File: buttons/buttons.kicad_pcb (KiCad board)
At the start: 2 copper layers, 9 parts, among them J1 header

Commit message: cleaned up directories, silkscreen
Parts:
- added H1: MountingHole, buttons:MountingHole_2.5mm_Pad, F.Cu at (109.9, 71.6)
- added H2: MountingHole, buttons:MountingHole_2.5mm_Pad, F.Cu at (141.9, 71.7)
- J1: footprint SamacSys_Parts:HDRV9W63P0X254_1X9_2286X369X950P -> buttons:header
- S1, S2: footprint SamacSys_Parts:OS103011MS8QP1 -> buttons:switch
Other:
- board outline added: 42 x 20.1 mm
- board text added: "ECE 477 Group 14 Switch Board Rev. 1"

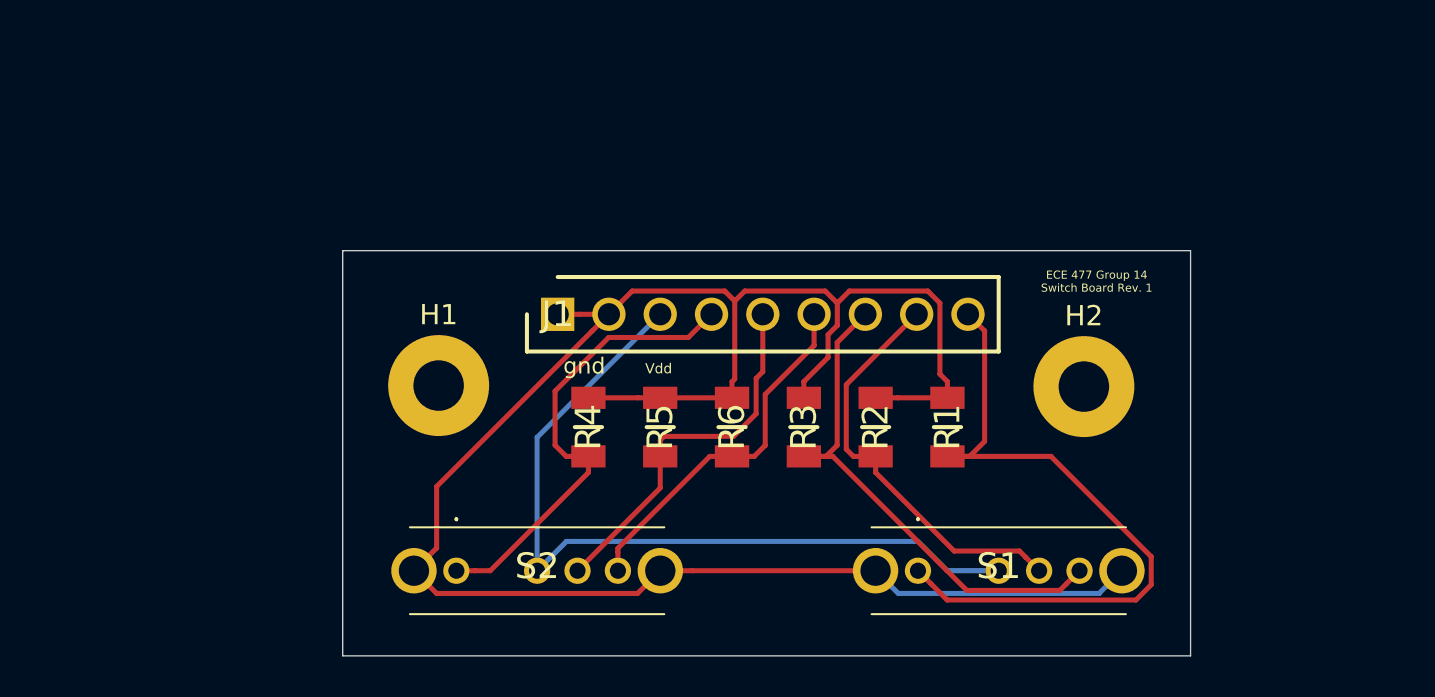
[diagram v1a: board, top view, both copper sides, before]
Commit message: Added reset button, fixed 7seg pin order
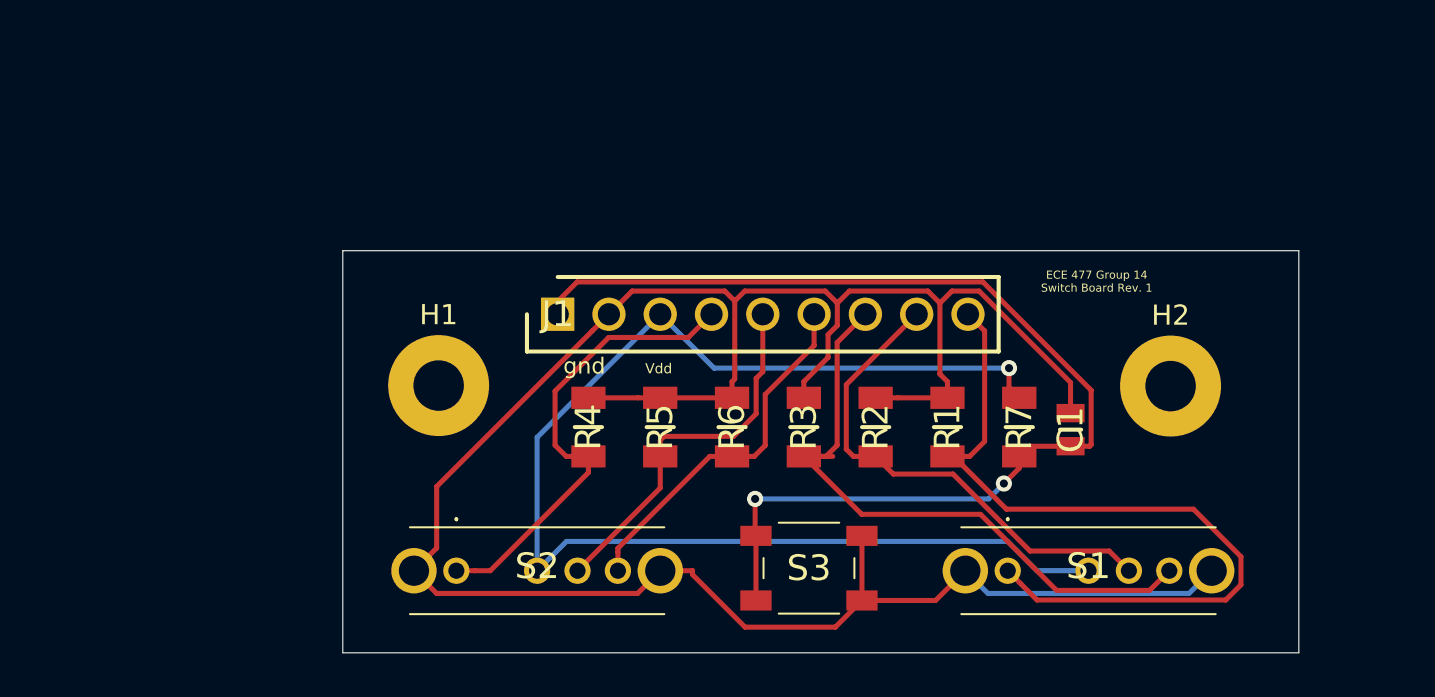
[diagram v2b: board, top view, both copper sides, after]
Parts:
- added C1: CL21B104KBCNNNC, SamacSys_Parts:CAPC2012X95N, F.Cu at (141.2, 73.8)
- added R7: 100k, SamacSys_Parts:RESC3116X70N, F.Cu at (138.7, 73.7)
- added S3: PTS647SM50SMTR2LFS, SamacSys_Parts:PTS647SM50SMTR2LFS, F.Cu at (128.3, 80.6)
- moved S1 4.44 mm to (142.1, 80.8)
- moved H2 4.29 mm to (146.2, 71.6)
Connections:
- J1 pad 1: /gnd -> Net-(C1-Pad1)
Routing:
- net Net-(C1-Pad1): track 0.00 -> 56.1 mm, vias 0 -> 2
- net /Vdd: track 39.3 -> 63.8 mm, vias 0 -> 1
- net /gnd: track 99.9 -> 117.6 mm
- net Net-(J1-Pad7): track 25.7 -> 31.6 mm
- net Net-(J1-Pad9): track 34.8 -> 39.2 mm
- net Net-(J1-Pad8): track 20.6 -> 24.6 mm
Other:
- board size 42 x 20.1 mm -> 47.3 x 19.9 mm

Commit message: final Rev1 changes. increased heatsink area, flipped LEDs again, increased button mount hole size
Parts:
- H1, H2: footprint buttons:MountingHole_2.5mm_Pad -> buttons:MountingHole_3.2mm_M3_Pad
- moved H2 2.18 mm to (147.9, 72.9)
- moved H1 1.37 mm to (109.7, 72.9)
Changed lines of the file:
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@@
-(kicad_pcb (version 20171130) (host pcbnew "(5.1.10)-1")
+(kicad_pcb (version 20171130) (host pcbnew "(5.1.5)-3")
   (general
     (thickness 1.6)
@@
     (add_net "Net-(J1-Pad9)")
   )
+  (module buttons:MountingHole_3.2mm_M3_Pad (layer F.Cu)
+    (at 147.9296 72.9234)
+    (descr "Mounting Hole 3.2mm, M3")
+    (tags "mounting hole 3.2mm m3")
+    (attr virtual)
+    (fp_text reference H2 (at 0 -4.2) (layer F.SilkS)
+      (effects (font (size 1 1) (thickness 0.15)))
+    )
+    (fp_text value MountingHole (at 0 4.2) (layer F.Fab)
+      (effects (font (size 1 1) (thickness 0.15)))
+    )
+    (fp_circle (center 0 0) (end 3.45 0) (layer F.CrtYd) (width 0.05))
+    (fp_circle (center 0 0) (end 3.2 0) (layer Cmts.User) (width 0.15))
+    (fp_text user %R (at 0.3 0) (layer F.Fab)
+      (effects (font (size 1 1) (thickness 0.15)))
+    )
+    (pad 1 thru_hole circle (at 0 0) (size 6.4 6.4) (drill 3.2) (layers *.Cu *.Mask))
+  )
+  (module buttons:MountingHole_3.2mm_M3_Pad (layer F.Cu)
+    (at 109.6518 72.9488)
+    (descr "Mounting Hole 3.2mm, M3")
+    (tags "mounting hole 3.2mm m3")
+    (attr virtual)
+    (fp_text reference H1 (at 0 -4.2) (layer F.SilkS)
+      (effects (font (size 1 1) (thickness 0.15)))
+    )
+    (fp_text value MountingHole (at 0 4.2) (layer F.Fab)
+      (effects (font (size 1 1) (thickness 0.15)))
+    )
+    (fp_circle (center 0 0) (end 3.45 0) (layer F.CrtYd) (width 0.05))
+    (fp_circle (center 0 0) (end 3.2 0) (layer Cmts.User) (width 0.15))
+    (fp_text user %R (at 0.3 0) (layer F.Fab)
+      (effects (font (size 1 1) (thickness 0.15)))
+    )
+    (pad 1 thru_hole circle (at 0 0) (size 6.4 6.4) (drill 3.2) (layers *.Cu *.Mask))
+  )
   (module SamacSys_Parts:PTS647SM50SMTR2LFS (layer F.Cu)
     (at 128.27 80.645)
@@
       (effects (font (size 1.27 1.27) (thickness 0.254)))
     )
+    (fp_line (start 2.25 -0.5) (end 2.25 0.5) (layer F.SilkS) (width 0.1))
+    (fp_line (start -1.5 2.25) (end 1.5 2.25) (layer F.SilkS) (width 0.1))
+    (fp_line (start -2.25 -0.5) (end -2.25 0.5) (layer F.SilkS) (width 0.1))
+    (fp_line (start -1.5 -2.25) (end 1.5 -2.25) (layer F.SilkS) (width 0.1))
+    (fp_line (start -4.4 3.25) (end -4.4 -3.25) (layer F.CrtYd) (width 0.1))
+    (fp_line (start 4.4 3.25) (end -4.4 3.25) (layer F.CrtYd) (width 0.1))
+    (fp_line (start 4.4 -3.25) (end 4.4 3.25) (layer F.CrtYd) (width 0.1))
+    (fp_line (start -4.4 -3.25) (end 4.4 -3.25) (layer F.CrtYd) (width 0.1))
+    (fp_line (start -2.25 2.25) (end -2.25 -2.25) (layer F.Fab) (width 0.2))
+    (fp_line (start 2.25 2.25) (end -2.25 2.25) (layer F.Fab) (width 0.2))
+    (fp_line (start 2.25 -2.25) (end 2.25 2.25) (layer F.Fab) (width 0.2))
+    (fp_line (start -2.25 -2.25) (end 2.25 -2.25) (layer F.Fab) (width 0.2))
     (fp_text user %R (at 0 0) (layer F.Fab)
       (effects (font (size 1.27 1.27) (thickness 0.254)))
     )
-    (fp_line (start -2.25 -2.25) (end 2.25 -2.25) (layer F.Fab) (width 0.2))
-    (fp_line (start 2.25 -2.25) (end 2.25 2.25) (layer F.Fab) (width 0.2))
-    (fp_line (start 2.25 2.25) (end -2.25 2.25) (layer F.Fab) (width 0.2))
-    (fp_line (start -2.25 2.25) (end -2.25 -2.25) (layer F.Fab) (width 0.2))
-    (fp_line (start -4.4 -3.25) (end 4.4 -3.25) (layer F.CrtYd) (width 0.1))
-    (fp_line (start 4.4 -3.25) (end 4.4 3.25) (layer F.CrtYd) (width 0.1))
-    (fp_line (start 4.4 3.25) (end -4.4 3.25) (layer F.CrtYd) (width 0.1))
-    (fp_line (start -4.4 3.25) (end -4.4 -3.25) (layer F.CrtYd) (width 0.1))
-    (fp_line (start -1.5 -2.25) (end 1.5 -2.25) (layer F.SilkS) (width 0.1))
-    (fp_line (start -2.25 -0.5) (end -2.25 0.5) (layer F.SilkS) (width 0.1))
-    (fp_line (start -1.5 2.25) (end 1.5 2.25) (layer F.SilkS) (width 0.1))
-    (fp_line (start 2.25 -0.5) (end 2.25 0.5) (layer F.SilkS) (width 0.1))
     (pad 4 smd rect (at 2.625 -1.6 90) (size 1 1.55) (layers F.Cu F.Paste F.Mask)
       (net 8 /gnd))
@@
     )
   )
-  (module buttons:MountingHole_2.5mm_Pad (layer F.Cu)
-    (at 146.177 71.628)
-    (descr "Mounting Hole 2.5mm")
-    (tags "mounting hole 2.5mm")
-    (attr virtual)
-    (fp_text reference H2 (at 0 -3.5) (layer F.SilkS)
-      (effects (font (size 1 1) (thickness 0.15)))
-    )
-    (fp_text value MountingHole (at 0 3.5) (layer F.Fab)
-      (effects (font (size 1 1) (thickness 0.15)))
-    )
-    (fp_circle (center 0 0) (end 2.5 0) (layer Cmts.User) (width 0.15))
-    (fp_circle (center 0 0) (end 2.75 0) (layer F.CrtYd) (width 0.05))
-    (fp_text user %R (at 0.3 0) (layer F.Fab)
-      (effects (font (size 1 1) (thickness 0.15)))
-    )
-    (pad 1 thru_hole circle (at 0 0) (size 5 5) (drill 2.5) (layers *.Cu *.Mask))
-  )
-  (module buttons:MountingHole_2.5mm_Pad (layer F.Cu)
-    (at 109.9312 71.6026)
-    (descr "Mounting Hole 2.5mm")
-    (tags "mounting hole 2.5mm")
-    (attr virtual)
-    (fp_text reference H1 (at 0 -3.5) (layer F.SilkS)
-      (effects (font (size 1 1) (thickness 0.15)))
-    )
-    (fp_text value MountingHole (at 0 3.5) (layer F.Fab)
-      (effects (font (size 1 1) (thickness 0.15)))
-    )
-    (fp_circle (center 0 0) (end 2.5 0) (layer Cmts.User) (width 0.15))
-    (fp_circle (center 0 0) (end 2.75 0) (layer F.CrtYd) (width 0.05))
-    (fp_text user %R (at 0.3 0) (layer F.Fab)
-      (effects (font (size 1 1) (thickness 0.15)))
-    )
-    (pad 1 thru_hole circle (at 0 0) (size 5 5) (drill 2.5) (layers *.Cu *.Mask))
-  )
   (module SamacSys_Parts:RESC3116X70N (layer F.Cu)
     (at 124.46 73.66 90)
@@
     )
   )
+  (gr_line (start 152.527 64.9224) (end 152.527 84.836) (layer Edge.Cuts) (width 0.05))
+  (gr_line (start 105.1814 84.836) (end 105.1814 64.9224) (layer Edge.Cuts) (width 0.05))
   (gr_line (start 152.527 84.836) (end 105.1814 84.836) (layer Edge.Cuts) (width 0.05))
-  (gr_line (start 152.527 64.9224) (end 152.527 84.836) (layer Edge.Cuts) (width 0.05))
   (gr_text "ECE 477 Group 14 \nSwitch Board Rev. 1" (at 142.5194 66.4464) (layer F.SilkS)
     (effects (font (size 0.4 0.4) (thickness 0.1)))
   )
-  (gr_line (start 105.1814 84.836) (end 105.1814 64.9224) (layer Edge.Cuts) (width 0.05))
   (gr_line (start 152.527 64.9224) (end 105.1814 64.9224) (layer Edge.Cuts) (width 0.05))
   (gr_text Vdd (at 120.8278 70.7644) (layer F.SilkS)
@@
   (segment (start 137.137999 81.896999) (end 147.088001 81.896999) (width 0.25) (layer B.Cu) (net 8))
   (segment (start 136.013 80.772) (end 137.137999 81.896999) (width 0.25) (layer B.Cu) (net 8))
-  (segment (start 109.832999 76.603001) (end 117.539001 68.896999) (width 0.25) (layer F.Cu) (net 8))
-  (segment (start 117.539001 68.896999) (end 118.364 68.072) (width 0.25) (layer F.Cu) (net 8))
-  (segment (start 109.832999 79.647001) (end 109.832999 76.603001) (width 0.25) (layer F.Cu) (net 8))
-  (segment (start 108.708 80.772) (end 109.832999 79.647001) (width 0.25) (layer F.Cu) (net 8))
   (segment (start 122.49899 80.958992) (end 125.105998 83.566) (width 0.25) (layer F.Cu) (net 8))
   (segment (start 122.49899 80.772) (end 122.49899 80.958992) (width 0.25) (layer F.Cu) (net 8))
@@
   (segment (start 141.224 71.449998) (end 136.696001 66.921999) (width 0.25) (layer F.Cu) (net 8))
   (segment (start 141.224 72.967) (end 141.224 71.449998) (width 0.25) (layer F.Cu) (net 8))
+  (segment (start 109.832999 79.647001) (end 108.708 80.772) (width 0.25) (layer F.Cu) (net 8))
+  (segment (start 113.792 75.688) (end 109.832999 79.647001) (width 0.25) (layer F.Cu) (net 8))
+  (segment (start 118.364 68.072) (end 113.792 72.644) (width 0.25) (layer F.Cu) (net 8))
+  (segment (start 113.792 72.644) (end 113.792 75.688) (width 0.25) (layer F.Cu) (net 8))
   (segment (start 139.187 74.607) (end 138.684 75.11) (width 0.25) (layer F.Cu) (net 9))
   (segment (start 141.224 74.607) (end 139.187 74.607) (width 0.25) (layer F.Cu) (net 9))

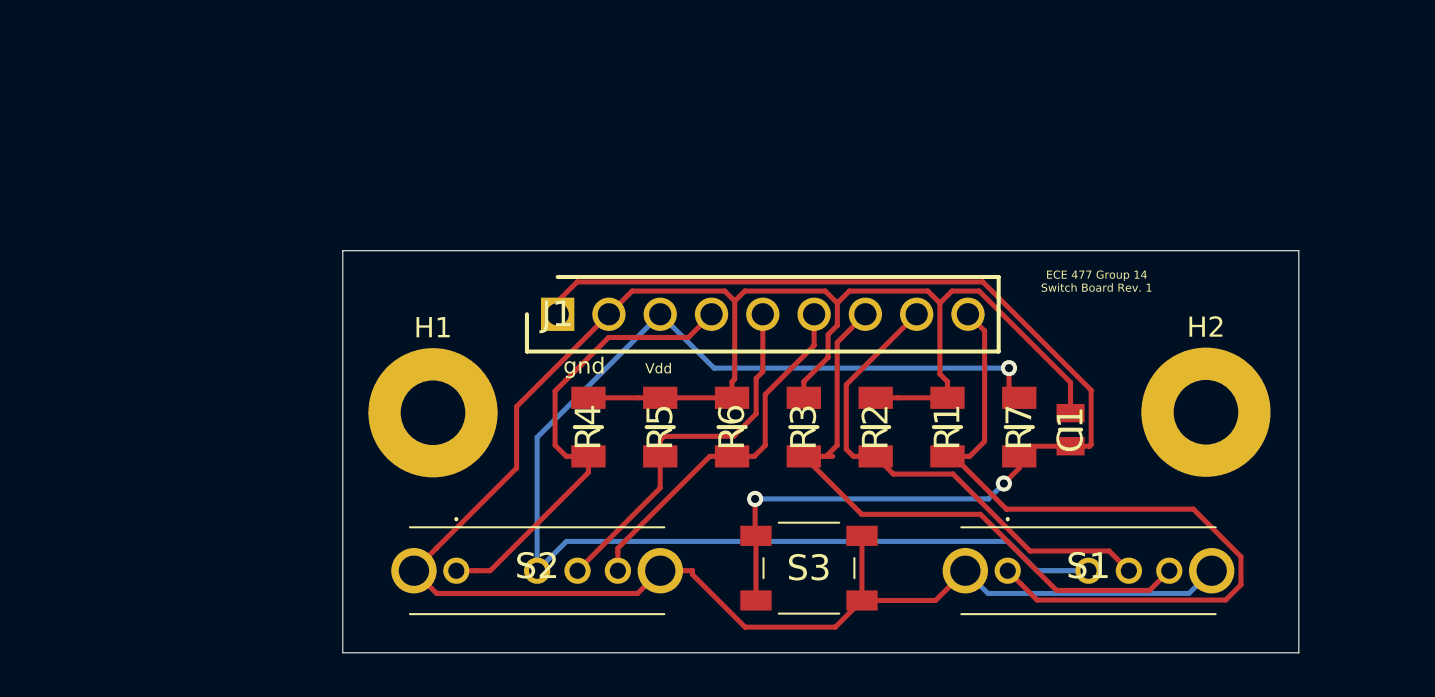
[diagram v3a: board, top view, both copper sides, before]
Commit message: added two more buttons
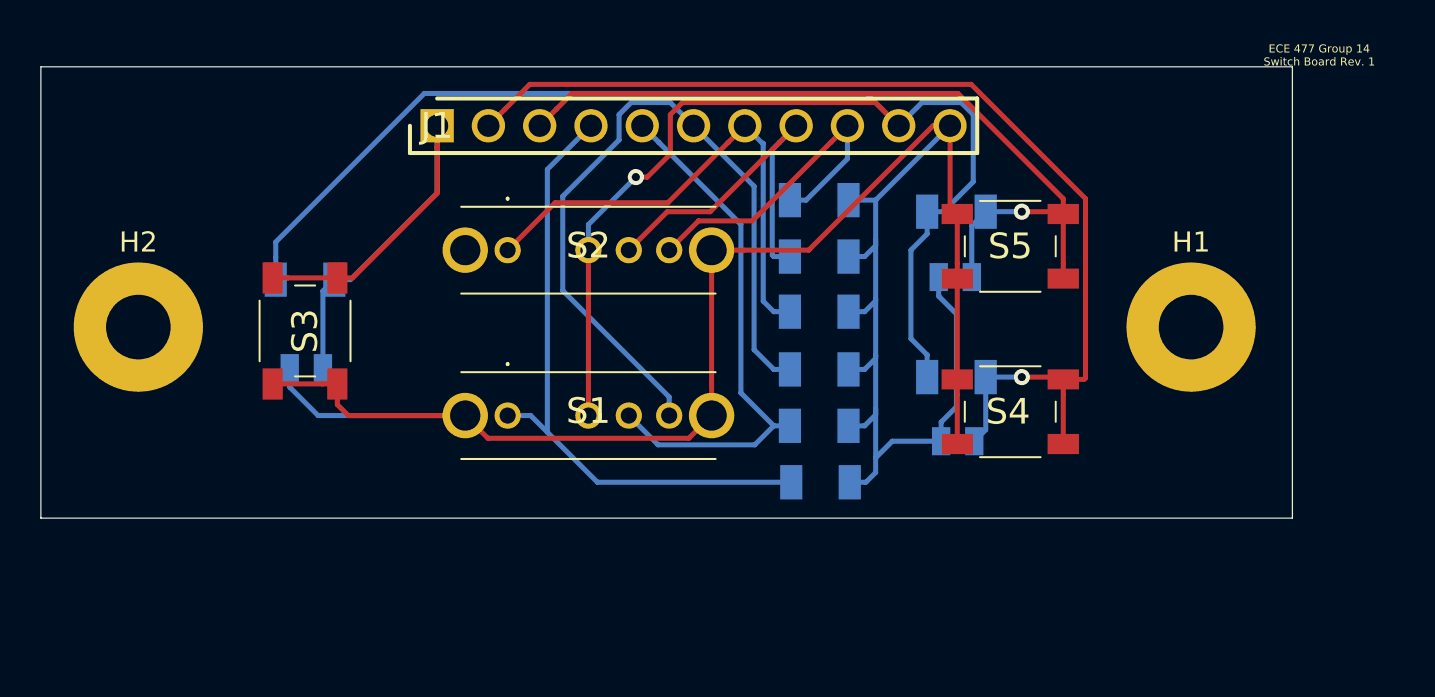
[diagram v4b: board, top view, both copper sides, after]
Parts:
- added C2: CL21B104KBCNNNC, SamacSys_Parts:CAPC2012X95N, B.Cu at (135.6, 74.4)
- added C3: CL21B104KBCNNNC, SamacSys_Parts:CAPC2012X95N, B.Cu at (135.5, 66.2)
- added R8: 100k, SamacSys_Parts:RESC3116X70N, B.Cu at (135.6, 71.2)
- added R9: 100k, SamacSys_Parts:RESC3116X70N, B.Cu at (135.6, 63.0)
- added S4: PTS647SM50SMTR2LFS, SamacSys_Parts:PTS647SM50SMTR2LFS, F.Cu at (138.2, 72.9)
- added S5: PTS647SM50SMTR2LFS, SamacSys_Parts:PTS647SM50SMTR2LFS, F.Cu at (138.2, 64.7)
- C1, R1, R2, R3, R4, R5, R6, R7: moved to B.Cu
- J1: value header -> 77311-862-11LF; footprint buttons:header -> buttons:HDRV11W62P0X254_1X11_2794X240X853P
- moved H2 53.0 mm to (95.1, 68.7)
- moved C1 38.0 mm to (103.4, 70.7), turned to 0 degrees
- moved H1 37.8 mm to (147.2, 68.7)
- moved R7 36.1 mm to (103.3, 66.4), turned to 180 degrees
- moved S3 27.6 mm to (103.3, 68.9), turned to 90 degrees
- moved S1 25.9 mm to (117.3, 73.1)
- moved S2 16.1 mm to (117.3, 64.9)
- moved R4 16.0 mm to (128.8, 62.4), turned to 0 degrees
- moved R5 11.5 mm to (128.8, 65.2), turned to 0 degrees
- moved J1 11.1 mm to (109.9, 58.7)
- moved R6 7.16 mm to (128.8, 67.9), turned to 0 degrees
- moved R1 6.85 mm to (128.8, 76.4), turned to 0 degrees
- moved R3 2.96 mm to (128.8, 70.8), turned to 0 degrees
- moved R2 2.79 mm to (128.8, 73.6), turned to 0 degrees
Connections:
- C1 pad 1: Net-(C1-Pad1) -> GND
- C1 pad 2: /gnd -> Net-(C1-Pad2)
- J1 pad 1: Net-(C1-Pad1) -> Net-(C1-Pad2)
- J1 pad 2: /gnd -> Net-(C2-Pad2)
- J1 pad 3: /Vdd -> Net-(C3-Pad2)
- R1 pad 1: Net-(J1-Pad9) -> Net-(J1-Pad4)
- R1 pad 2: /gnd -> GND
- R2 pad 1: Net-(J1-Pad8) -> Net-(J1-Pad5)
- R2 pad 2: /gnd -> GND
- R3 pad 1: Net-(J1-Pad7) -> Net-(J1-Pad6)
- R3 pad 2: /gnd -> GND
- R4 pad 1: Net-(J1-Pad4) -> Net-(J1-Pad9)
- R4 pad 2: /gnd -> GND
- R5 pad 1: Net-(J1-Pad5) -> Net-(J1-Pad8)
- R5 pad 2: /gnd -> GND
- R6 pad 1: Net-(J1-Pad6) -> Net-(J1-Pad7)
- R6 pad 2: /gnd -> GND
- R7 pad 1: Net-(C1-Pad1) -> Net-(C1-Pad2)
- R7 pad 2: /Vdd -> +3V3
- S1 pad 1: Net-(J1-Pad9) -> Net-(J1-Pad4)
- S1 pad 2: /Vdd -> +3V3
- S1 pad 3: Net-(J1-Pad8) -> Net-(J1-Pad5)
- S1 pad 4: Net-(J1-Pad7) -> Net-(J1-Pad6)
- S1 pad 5: /gnd -> GND
- S1 pad 6: /gnd -> GND
- S2 pad 1: Net-(J1-Pad4) -> Net-(J1-Pad7)
- S2 pad 2: /Vdd -> +3V3
- S2 pad 3: Net-(J1-Pad5) -> Net-(J1-Pad8)
- S2 pad 4: Net-(J1-Pad6) -> Net-(J1-Pad9)
- S2 pad 5: /gnd -> GND
- S2 pad 6: /gnd -> GND
- S3 pad 1: Net-(C1-Pad1) -> GND
- S3 pad 2: Net-(C1-Pad1) -> GND
- S3 pad 3: /gnd -> Net-(C1-Pad2)
- S3 pad 4: /gnd -> Net-(C1-Pad2)
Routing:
- net /gnd: track 117.6 -> 0.00 mm
- net GND: track 0.00 -> 113.7 mm
- net +3V3: track 0.00 -> 84.9 mm, vias 0 -> 1
- net /Vdd: track 63.8 -> 0.00 mm, vias 1 -> 0
- net Net-(C1-Pad1): track 56.1 -> 0.00 mm, vias 2 -> 0
- net Net-(C2-Pad2): track 0.00 -> 53.3 mm, vias 0 -> 1
- net Net-(C3-Pad2): track 0.00 -> 40.1 mm, vias 0 -> 1
- net Net-(C1-Pad2): track 0.00 -> 28.0 mm
- net Net-(J1-Pad9): track 39.2 -> 16.7 mm
- net Net-(J1-Pad6): track 18.0 -> 37.2 mm
- net Net-(J1-Pad4): track 23.2 -> 31.5 mm
- net Net-(J1-Pad5): track 18.5 -> 26.5 mm
- net Net-(J1-Pad7): track 31.6 -> 24.9 mm
- net Net-(J1-Pad8): track 24.6 -> 18.6 mm
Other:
- board size 47.3 x 19.9 mm -> 62 x 22.4 mm
- board text removed: "Vdd"
- board text removed: "gnd"
